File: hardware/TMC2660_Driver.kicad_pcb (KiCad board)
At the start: 4 copper layers, 36.7 x 39.4 mm, 27 parts, among them J1 PCIe_Stepper, J2 Conn_01x04_Male, U1 TMC2660, U2 74LVC1G06

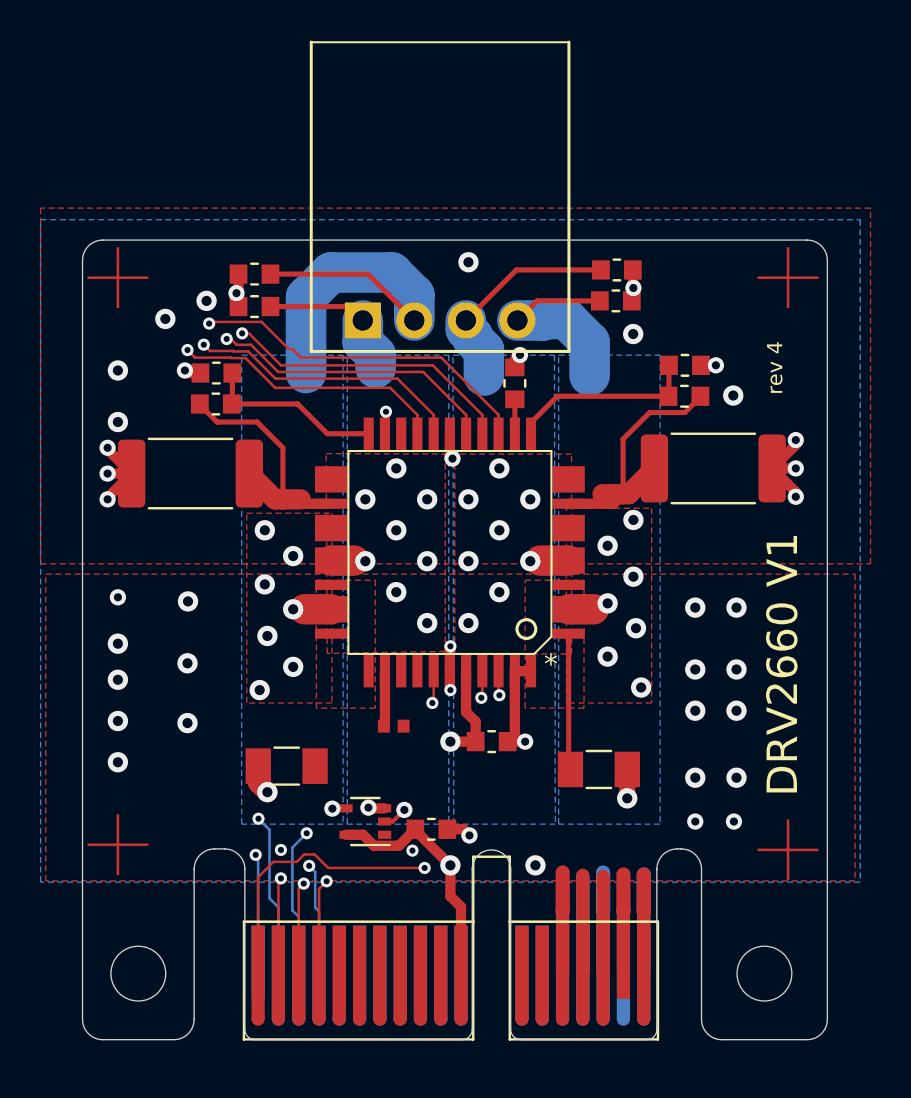
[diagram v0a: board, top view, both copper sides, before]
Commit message: Added more dimensions.
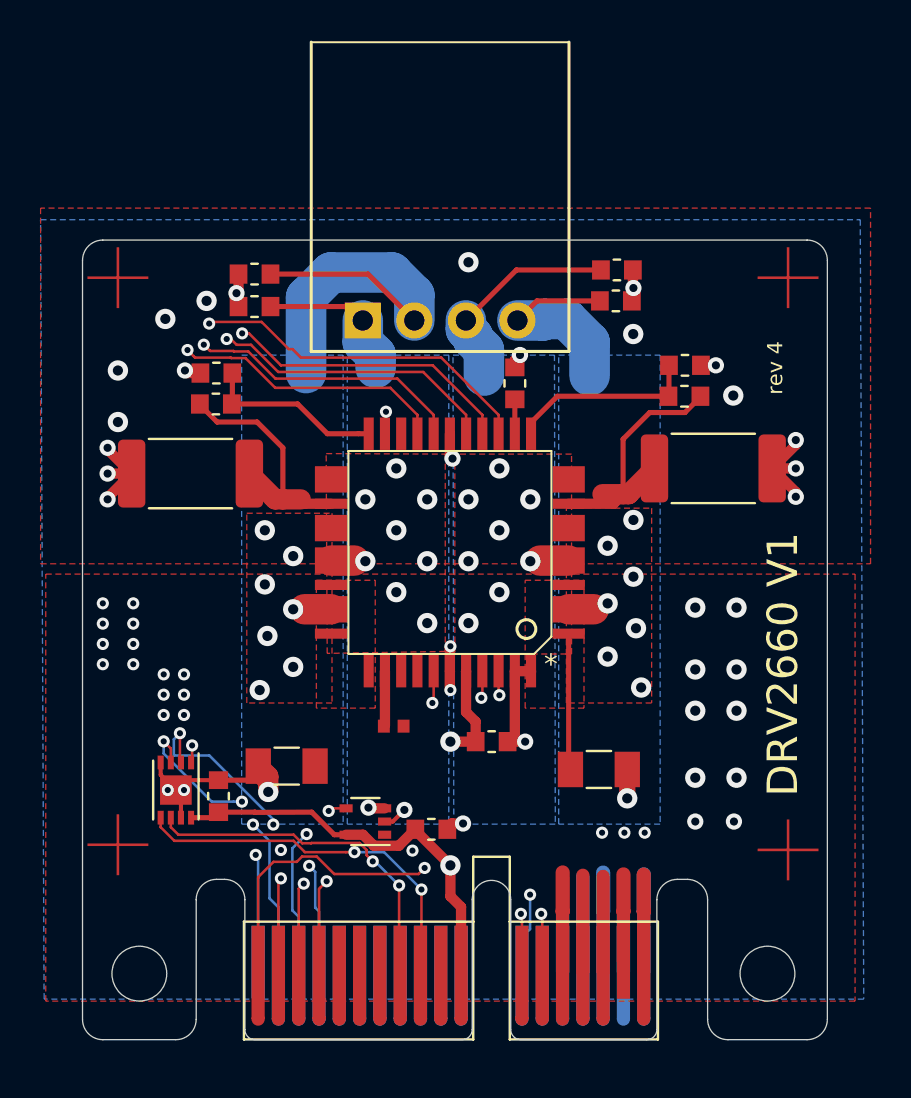
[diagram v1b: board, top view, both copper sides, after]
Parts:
- added C14: 0.1uF, PrntrBoardV2:C_0603_1608Metric, F.Cu at (115.7, 102.0)
- added U3: 24LC02, PrntrBoardV2:TDFN-8-1EP_3x2mm_P0.5mm_EP1.56x1.45mm, F.Cu at (113.6, 101.7)
- moved H2 0.15 mm to (142.8, 110.7)
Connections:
- J1 pad A12: (no net) -> /ID_1
- J1 pad B12: (no net) -> /ID_0
- J1 pad B13: (no net) -> /ID_2
- J1 pad B8: (no net) -> /SCL
- J1 pad B9: (no net) -> /SDA
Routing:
- net /ID_0: track 0.00 -> 29.3 mm, vias 0 -> 2
- net /ID_1: track 0.00 -> 28.2 mm, vias 0 -> 3
- net /ID_2: track 0.00 -> 28.0 mm, vias 0 -> 3
- net /SDA: track 0.00 -> 18.7 mm, vias 0 -> 2
- net /SCL: track 0.00 -> 17.4 mm, vias 0 -> 2
- net VCC: track 23.0 -> 31.6 mm
- net GND: track 53.8 -> 61.6 mm, vias 41 -> 56
- net /V_MOTORS: vias 5 -> 0
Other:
- outline, holes or cut-outs redrawn
- board text added: "(c) iQury.us Dec 2019"
- board text removed: "(c) iQury.us Nov 2019"

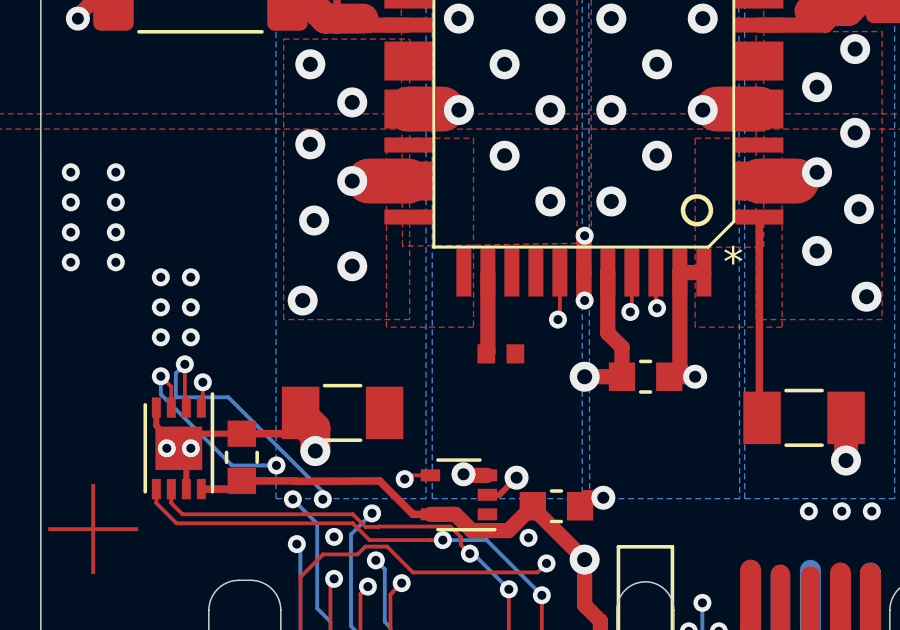
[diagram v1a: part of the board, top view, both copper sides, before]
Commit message: Route a mystery trace on the 2660 driver.
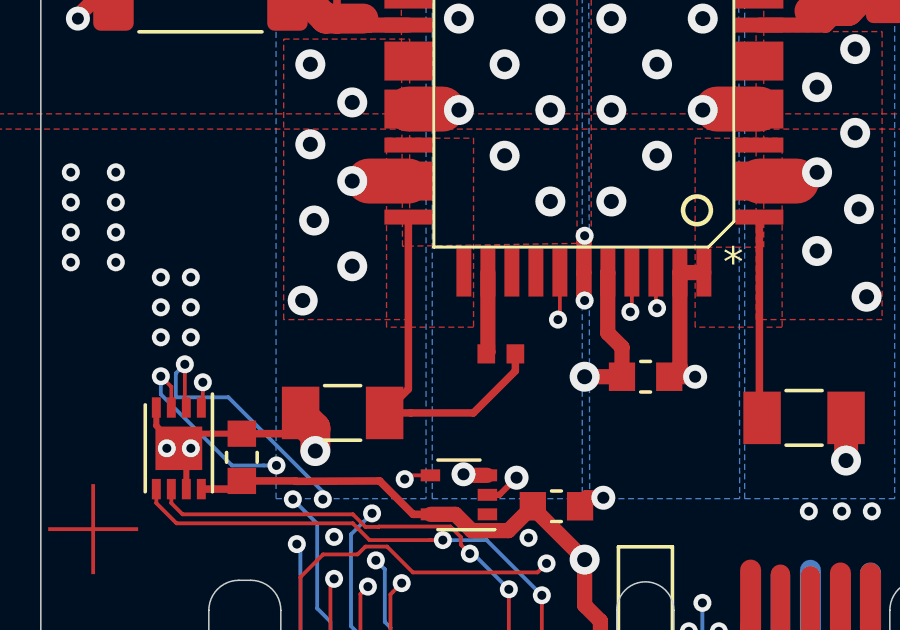
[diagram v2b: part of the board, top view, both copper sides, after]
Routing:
- net /V_MOTORS: track 30.6 -> 43.0 mm

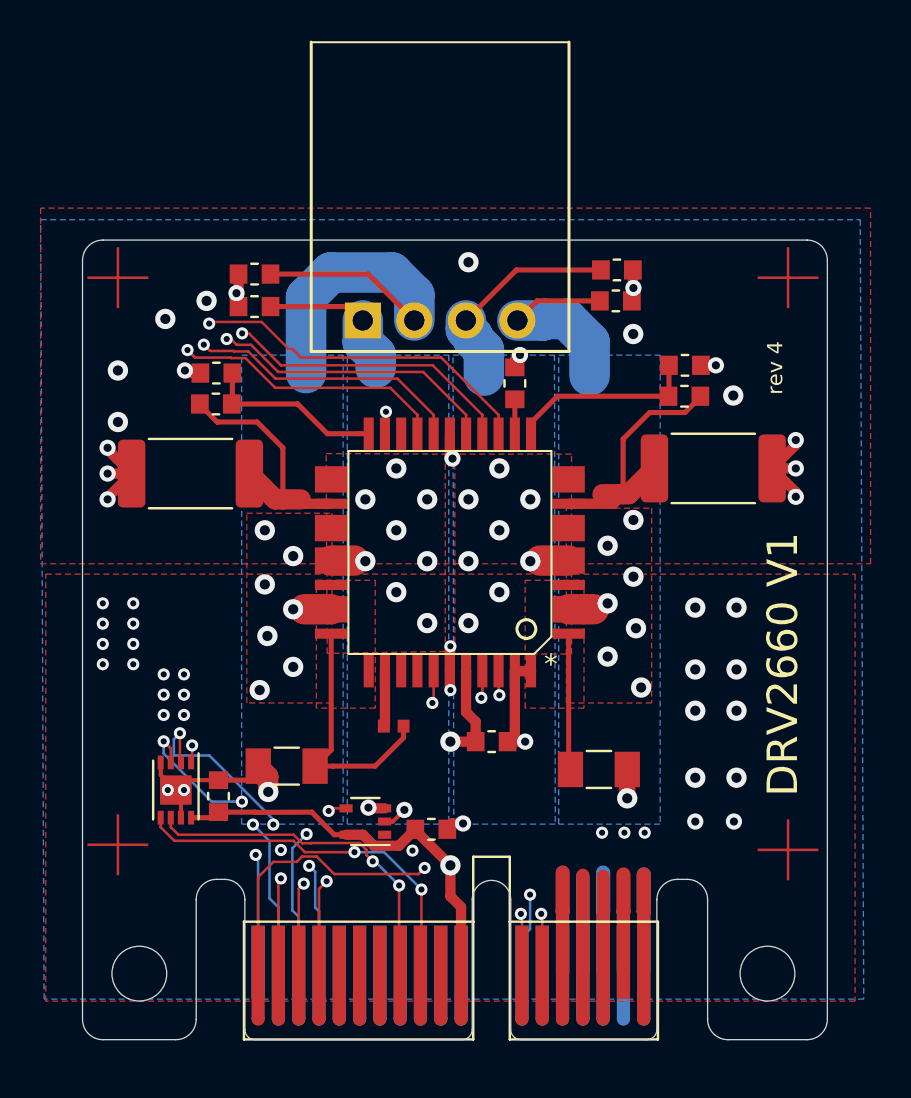
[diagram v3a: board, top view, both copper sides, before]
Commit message: Add electrolytic CAP on the drivers.
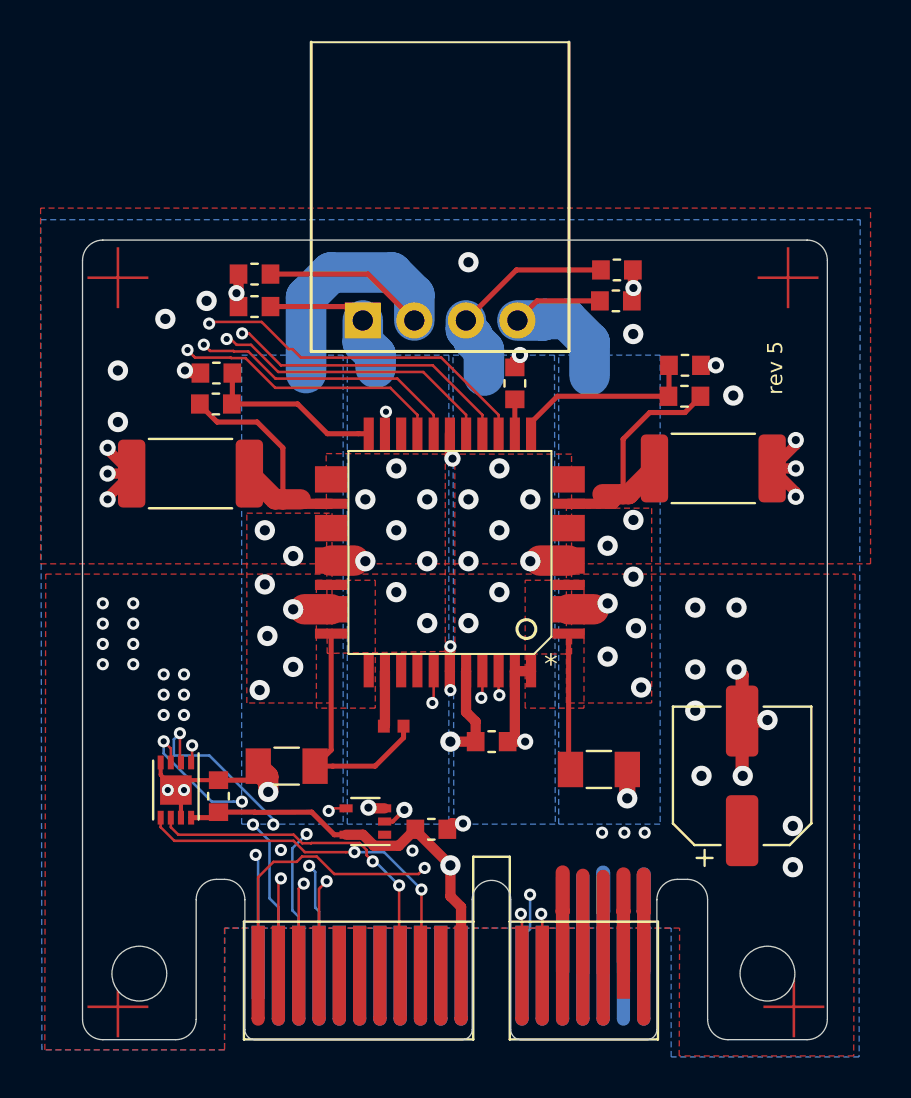
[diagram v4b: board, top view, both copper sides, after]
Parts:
- added C13: 100uF 35V, Capacitor_SMD:CP_Elec_6.3x5.7, F.Cu at (141.5, 101.0)
- moved FID2 7.99 mm to (110.7, 112.4)
- moved FID4 7.74 mm to (144.1, 112.4)
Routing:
- net GND: track 61.6 -> 68.3 mm
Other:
- board text added: "(c) iQury.us Mar 2020"
- board text added: "rev 5"
- board text removed: "(c) iQury.us Dec 2019"
- board text removed: "rev 4"

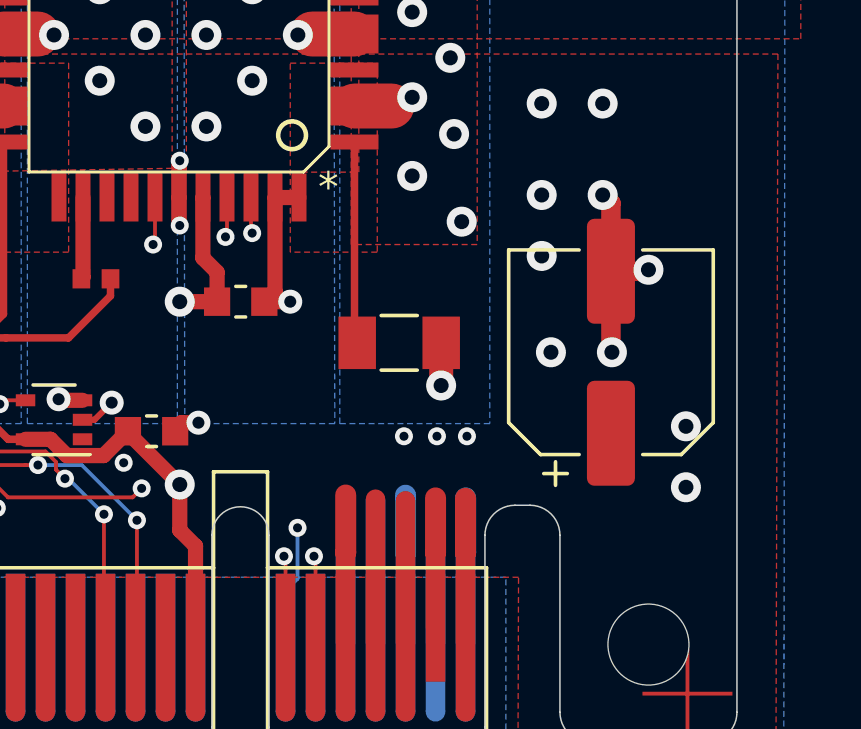
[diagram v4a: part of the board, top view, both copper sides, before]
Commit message: Fix label positions.
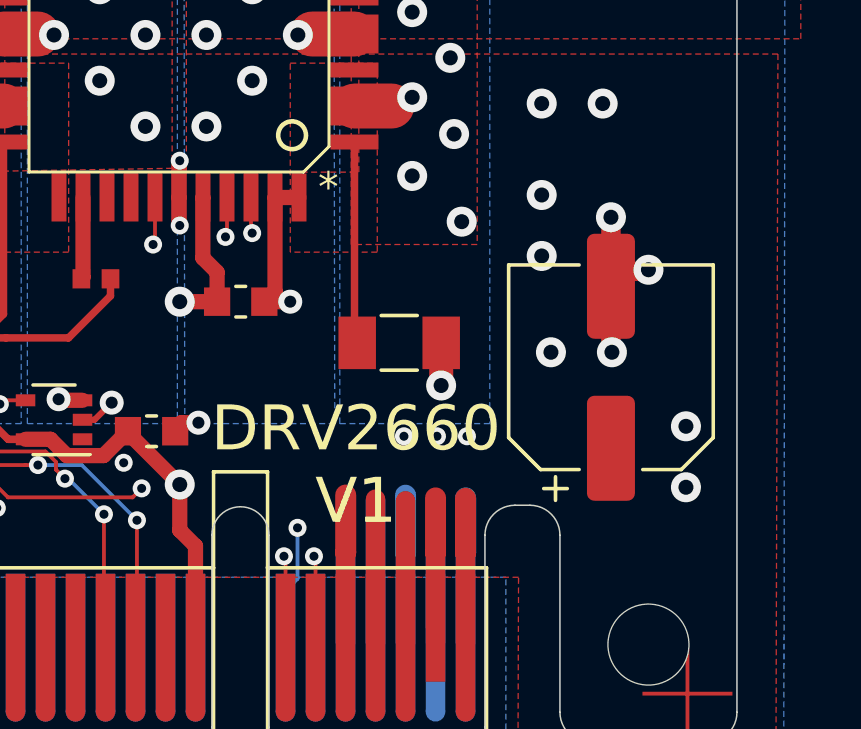
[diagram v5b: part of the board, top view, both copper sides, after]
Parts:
- C13: footprint Capacitor_SMD:CP_Elec_6.3x5.7 -> Capacitor_SMD:CP_Elec_6.3x7.7
- moved C13 0.50 mm to (141.5, 101.5)

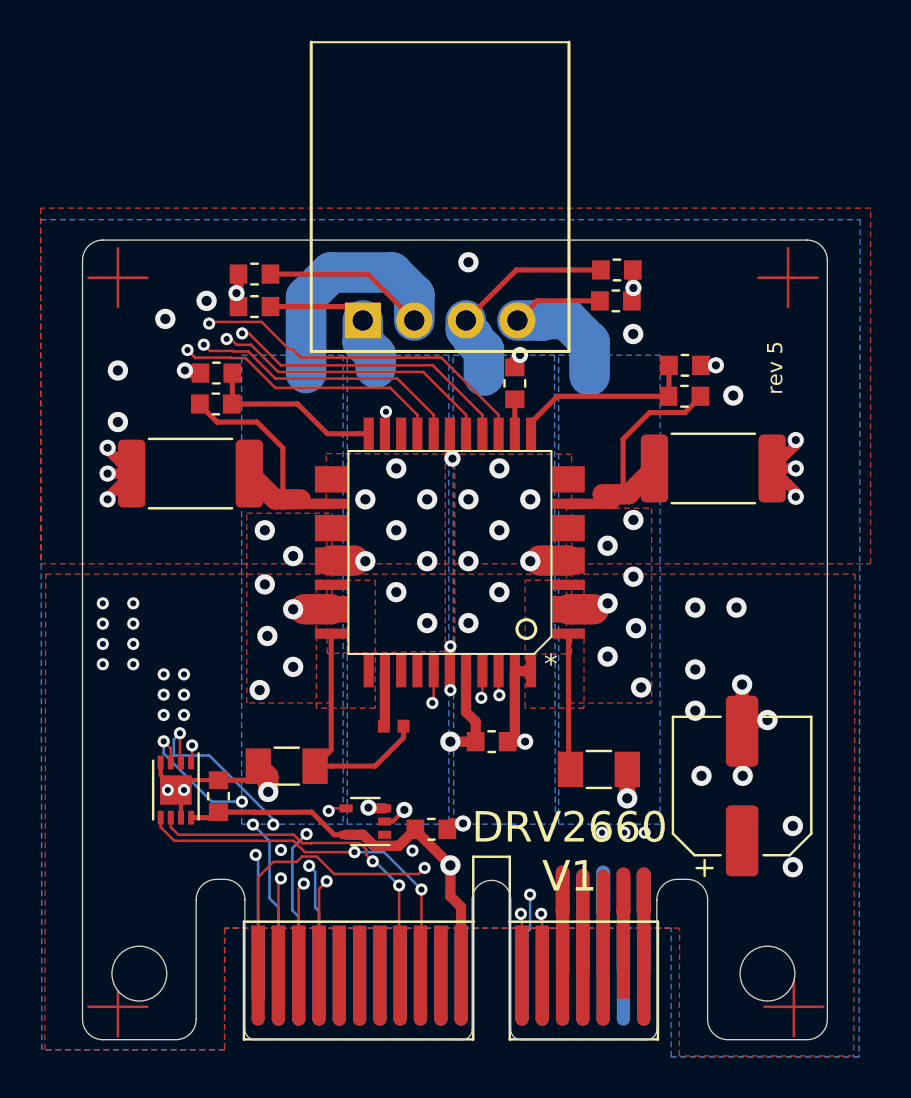
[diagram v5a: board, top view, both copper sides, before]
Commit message: Update TMC2660 pcb.
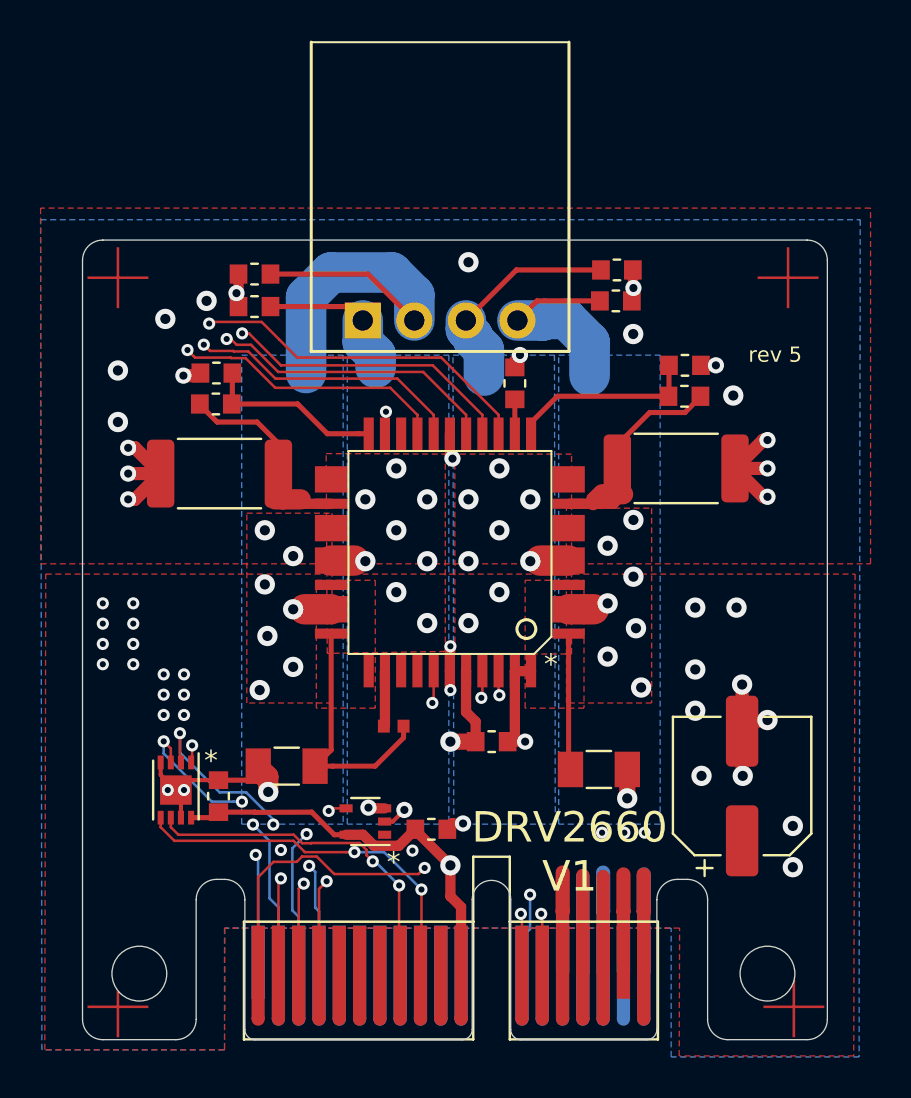
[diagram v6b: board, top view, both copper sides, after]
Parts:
- moved R4 1.83 mm to (138.2, 85.9)
- moved R2 1.43 mm to (115.8, 86.1)
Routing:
- net GND: track 67.9 -> 70.2 mm
- net /ID_0: track 29.3 -> 27.1 mm
- net Net-(R1-Pad2): track 12.2 -> 10.4 mm
- net Net-(R3-Pad2): track 13.4 -> 11.9 mm
- net /MOSI: track 51.8 -> 50.5 mm
- net /SCK: track 48.9 -> 47.6 mm
- net /~CS: track 48.1 -> 47.3 mm
- net /~ENABLE: track 48.2 -> 47.6 mm
- net /ID_1: track 28.2 -> 27.7 mm
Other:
- rule trace_min: 0.0889 -> 0.127
- board text added: "(c) iQury.us Apr 2020"
- board text removed: "(c) iQury.us Mar 2020"

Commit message: Updated driver PCBs.
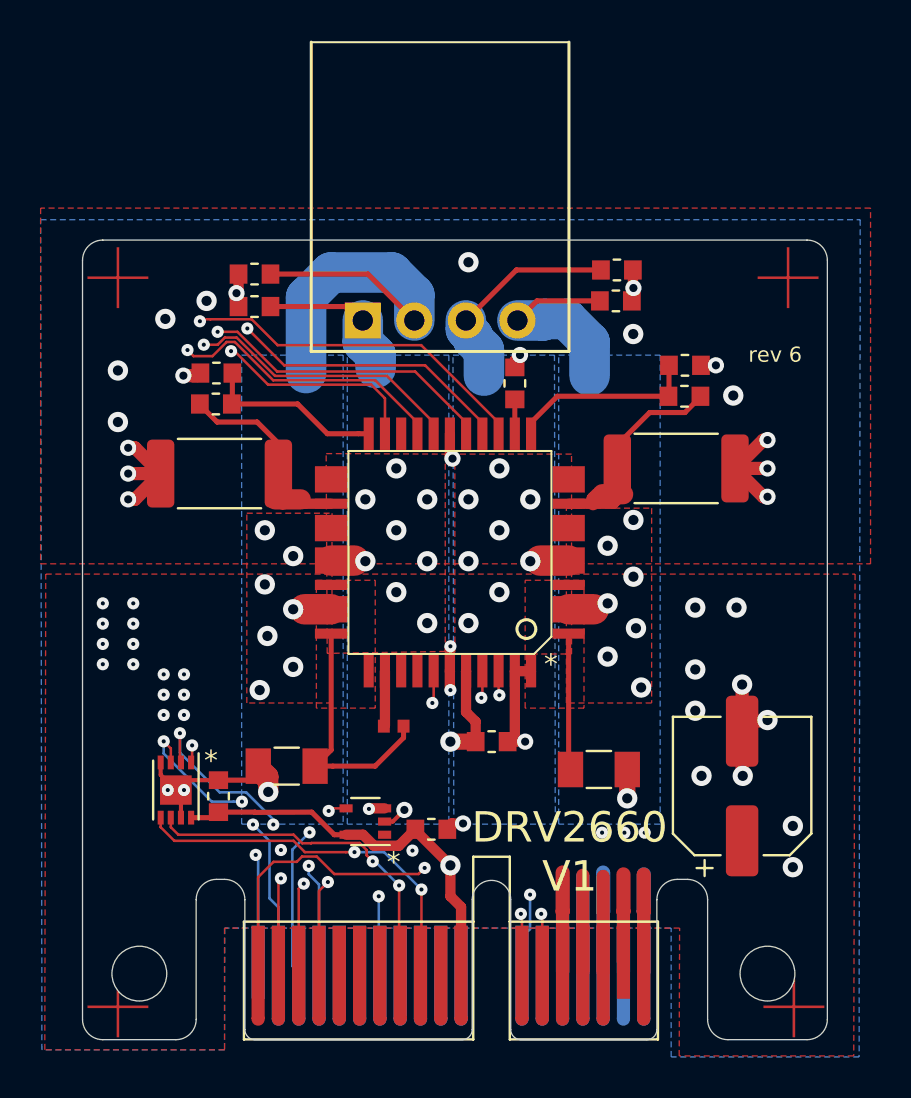
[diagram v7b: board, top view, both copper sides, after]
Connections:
- J1 pad A7: (no net) -> /CLOCK
- U1 pad 21: GND -> /CLOCK
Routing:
- net /CLOCK: track 0.00 -> 46.2 mm, vias 0 -> 2
- net GND: track 70.2 -> 69.1 mm, vias 56 -> 55
- net /SCK: track 47.6 -> 48.5 mm
- net /MISO: track 47.7 -> 48.3 mm
- net /MOSI: track 50.5 -> 51.1 mm
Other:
- rule trace_min: 0.127 -> 0.0762
- board text added: "(c) iQury.us May 2020"
- board text added: "rev 6"
- board text removed: "(c) iQury.us Apr 2020"
- board text removed: "rev 5"
